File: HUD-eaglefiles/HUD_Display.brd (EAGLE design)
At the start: 71.1 x 45.7 mm, 7 parts

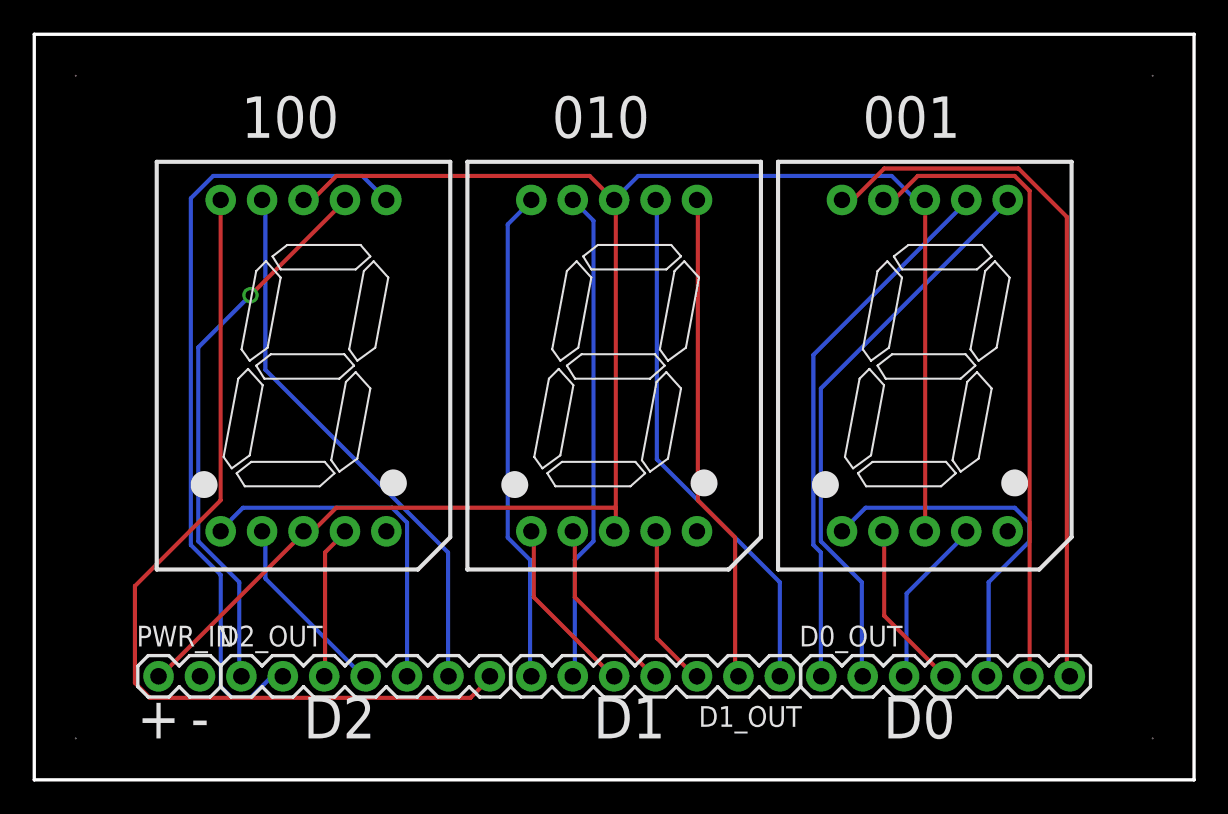
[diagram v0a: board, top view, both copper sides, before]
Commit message: modified the display layout to make single layer and added the silk screen text
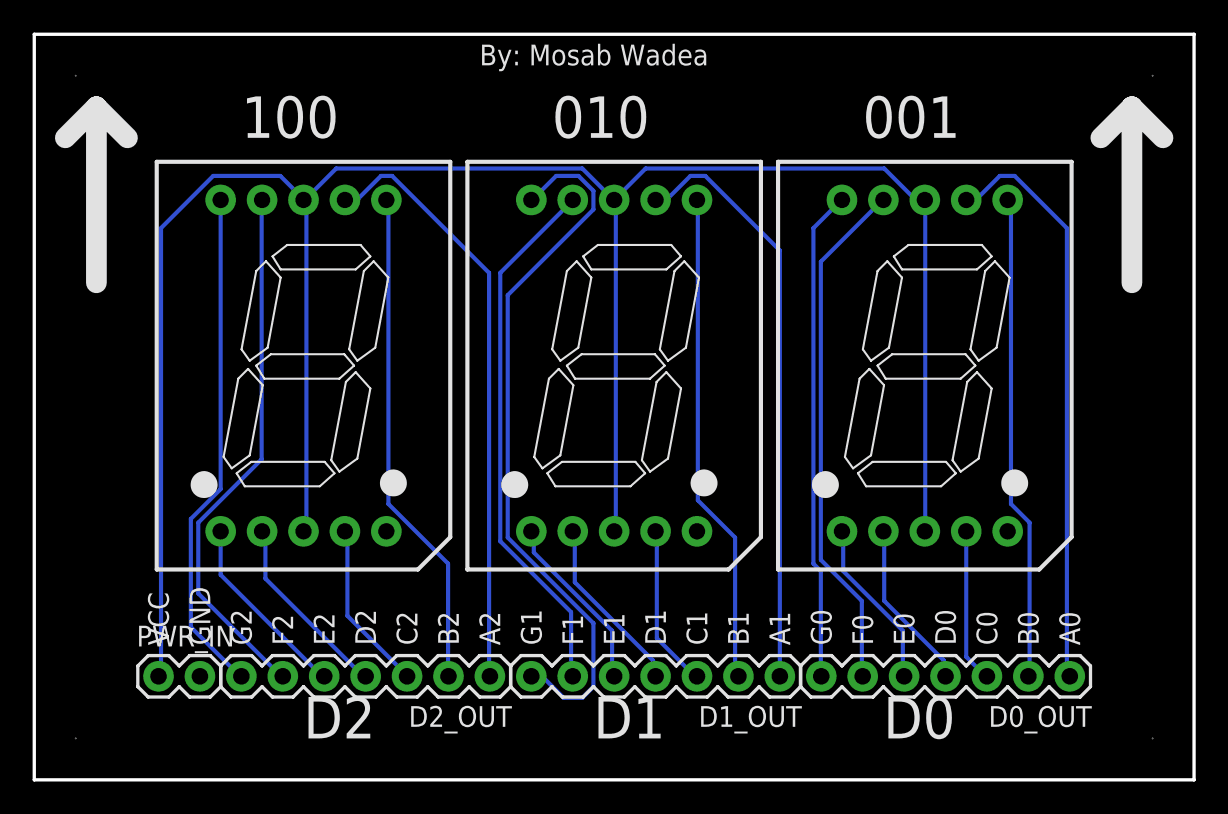
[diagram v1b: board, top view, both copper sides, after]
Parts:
- moved D0_OUT 15.2 mm to (63.5, 6.35), turned to 180 degrees
- moved D2_OUT 15.2 mm to (27.9, 6.35), turned to 180 degrees
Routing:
- net VCC: track 113.6 -> 140.8 mm
- net DO_OUT: track 54.5 -> 31.3 mm
- net N$2: track 48.5 -> 30.8 mm
- net N$21: track 44.1 -> 30.1 mm
- net N$14: track 30.4 -> 44.2 mm
- net N$19: track 23.0 -> 10.5 mm
- net N$5: track 21.9 -> 11.6 mm
- net N$20: track 39.8 -> 31.9 mm
- net N$16: track 35.0 -> 29.8 mm
- net N$8: track 32.4 -> 36.2 mm
- net D1_OUT: track 30.3 -> 32.9 mm
- net N$1: track 34.1 -> 36.7 mm, vias 1 -> 0
- net N$15: track 33.3 -> 35.8 mm
- net N$3: track 9.40 -> 10.5 mm
- net N$17: track 10.5 -> 9.45 mm
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- added copper zone on layer 16, net N$7
- removed copper zone on layer 16, net N$13
- removed copper zone on layer 1, net N$7
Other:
- board text added: "A0"
- board text added: "A1"
- board text added: "A2"
- board text added: "B0"
- board text added: "B1"
- board text added: "B2"
- board text added: "By: Mosab Wadea"
- board text added: "C0"
- board text added: "C1"
- board text added: "C2"
- board text added: "E0"
- board text added: "E1"
- board text added: "E2"
- board text added: "F0"
- board text added: "F1"
- board text added: "F2"
- board text added: "G0"
- board text added: "G1"
- board text added: "G2"
- board text added: "GND"
- board text added: "VCC"
- board text removed: "+"
- board text removed: "-"
